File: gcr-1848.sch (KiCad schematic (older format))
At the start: 12 parts, among them U1 LT6010

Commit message: Annotated some components and added a few Greek letters
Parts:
- C1: value 0.1uF -> 0.1μF
- C2, C3: value 33uF -> 33μF
- R3, R4: renamed from R?; value 220M -> 220MΩ
- gave numbers to parts that had none: 2
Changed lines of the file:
@@
 $EndComp
 $Comp
-L US_R R?
+L US_R R4
 U 1 1 5B46BAAD
 P 4350 3825
-F 0 "R?" H 4350 3725 60  0000 C CNN
-F 1 "220M" H 4350 3925 60  0000 C CNN
+F 0 "R4" H 4350 3725 60  0000 C CNN
+F 1 "220MΩ" H 4350 3925 60  0000 C CNN
 F 2 "" H 4350 3925 60  0001 C CNN
 F 3 "" H 4350 3925 60  0001 C CNN
@@
 $EndComp
 $Comp
-L US_R R?
+L US_R R3
 U 1 1 5B46BF5B
 P 4175 3250
-F 0 "R?" H 4175 3150 60  0000 C CNN
-F 1 "220M" H 4175 3350 60  0000 C CNN
+F 0 "R3" H 4175 3150 60  0000 C CNN
+F 1 "220MΩ" H 4175 3350 60  0000 C CNN
 F 2 "" H 4175 3350 60  0001 C CNN
 F 3 "" H 4175 3350 60  0001 C CNN
@@
 P 4575 5125
 F 0 "C1" H 4575 5000 60  0000 C CNN
-F 1 "0.1uF" H 4575 5250 60  0000 C CNN
+F 1 "0.1μF" H 4575 5250 60  0000 C CNN
 F 2 "" H 4575 5250 60  0001 C CNN
 F 3 "" H 4575 5250 60  0001 C CNN
@@
 $EndComp
 $Comp
-L CAPSL C?
+L CAPSL C4
 U 1 1 5B46D889
 P 4100 4350
-F 0 "C?" H 4100 4200 60  0000 C CNN
+F 0 "C4" H 4100 4200 60  0000 C CNN
 F 1 "CPLT" H 4100 4500 60  0000 C CNN
 F 2 "" H 4100 4475 60  0001 C CNN
@@
 $EndComp
 $Comp
-L XLR_MALE J?
+L XLR_MALE J1
 U 1 1 5B46DD1A
 P 4200 6700
-F 0 "J?" H 4200 6925 60  0000 C CNN
+F 0 "J1" H 4200 6925 60  0000 C CNN
 F 1 "XLR_MALE" H 4200 6475 60  0000 C CNN
 F 2 "" H 4200 6700 60  0001 C CNN
@@
 P 4650 6675
 F 0 "C3" H 4650 6550 60  0000 C CNN
-F 1 "33uF" H 4650 6800 60  0000 C CNN
+F 1 "33μF" H 4650 6800 60  0000 C CNN
 F 2 "" H 4650 6800 60  0001 C CNN
 F 3 "" H 4650 6800 60  0001 C CNN
@@
 P 3775 6025
 F 0 "C2" H 3775 5900 60  0000 C CNN
-F 1 "33uF" H 3775 6150 60  0000 C CNN
+F 1 "33μF" H 3775 6150 60  0000 C CNN
 F 2 "" H 3775 6150 60  0001 C CNN
 F 3 "" H 3775 6150 60  0001 C CNN

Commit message: Laid out components on PCB
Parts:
- C1: footprint (none) -> Capacitors_SMD:C_0805
- C2, C3: footprint (none) -> Capacitors_SMD:C_2220
- D1, D2: footprint (none) -> Diodes_SMD:SOD-123
- R1, R2, R3, R4: footprint (none) -> Resistors_SMD:R_0805
- U1: footprint (none) -> Housings_SOIC:SOIC-8_3.9x4.9mm_Pitch1.27mm
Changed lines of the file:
@@
 $EndDescr
 $Comp
-L Earth #PWR?
+L Earth #PWR01
 U 1 1 5B46BA91
 P 4100 4475
-F 0 "#PWR?" H 4100 4225 50  0001 C CNN
+F 0 "#PWR01" H 4100 4225 50  0001 C CNN
 F 1 "Earth" H 4100 4325 50  0001 C CNN
 F 2 "" H 4100 4475 50  0000 C CNN
@@
 F 0 "R4" H 4350 3725 60  0000 C CNN
 F 1 "220MΩ" H 4350 3925 60  0000 C CNN
-F 2 "" H 4350 3925 60  0001 C CNN
+F 2 "Resistors_SMD:R_0805" H 4350 3925 60  0001 C CNN
 F 3 "" H 4350 3925 60  0001 C CNN
 	1    4350 3825
@@
 F 0 "D2" H 4000 3950 60  0000 C CNN
 F 1 "12V" H 4000 3700 60  0000 C CNN
-F 2 "" H 4000 3825 60  0001 C CNN
+F 2 "Diodes_SMD:SOD-123" H 4000 3825 60  0001 C CNN
 F 3 "" H 4000 3825 60  0001 C CNN
 	1    4000 3825
@@
 $EndComp
 $Comp
-L Earth #PWR?
+L Earth #PWR02
 U 1 1 5B46BF2C
 P 4000 4000
-F 0 "#PWR?" H 4000 3750 50  0001 C CNN
+F 0 "#PWR02" H 4000 3750 50  0001 C CNN
 F 1 "Earth" H 4000 3850 50  0001 C CNN
 F 2 "" H 4000 4000 50  0000 C CNN
@@
 F 0 "R3" H 4175 3150 60  0000 C CNN
 F 1 "220MΩ" H 4175 3350 60  0000 C CNN
-F 2 "" H 4175 3350 60  0001 C CNN
+F 2 "Resistors_SMD:R_0805" H 4175 3350 60  0001 C CNN
 F 3 "" H 4175 3350 60  0001 C CNN
 	1    4175 3250
@@
 $EndComp
 $Comp
-L Earth #PWR?
+L Earth #PWR03
 U 1 1 5B46C6B1
 P 3875 4950
-F 0 "#PWR?" H 3875 4700 50  0001 C CNN
+F 0 "#PWR03" H 3875 4700 50  0001 C CNN
 F 1 "Earth" H 3875 4800 50  0001 C CNN
 F 2 "" H 3875 4950 50  0000 C CNN
@@
 F 0 "C1" H 4575 5000 60  0000 C CNN
 F 1 "0.1μF" H 4575 5250 60  0000 C CNN
-F 2 "" H 4575 5250 60  0001 C CNN
+F 2 "Capacitors_SMD:C_0805" H 4575 5250 60  0001 C CNN
 F 3 "" H 4575 5250 60  0001 C CNN
 	1    4575 5125
@@
 $EndComp
 $Comp
-L Earth #PWR?
+L Earth #PWR04
 U 1 1 5B46C778
 P 4650 5400
-F 0 "#PWR?" H 4650 5150 50  0001 C CNN
+F 0 "#PWR04" H 4650 5150 50  0001 C CNN
 F 1 "Earth" H 4650 5250 50  0001 C CNN
 F 2 "" H 4650 5400 50  0000 C CNN
@@
 F 0 "U1" H 4300 4970 50  0000 C CNN
 F 1 "LT6010" H 4225 4825 50  0000 L CNN
-F 2 "" H 4175 5075 50  0000 C CNN
+F 2 "Housings_SOIC:SOIC-8_3.9x4.9mm_Pitch1.27mm" H 4175 5075 50  0001 C CNN
 F 3 "" H 4275 5175 50  0000 C CNN
 	1    4225 4975
@@
 $EndComp
 $Comp
-L +24V #PWR?
+L +24V #PWR05
 U 1 1 5B46CDAE
 P 4575 4800
-F 0 "#PWR?" H 4575 4650 50  0001 C CNN
+F 0 "#PWR05" H 4575 4650 50  0001 C CNN
 F 1 "+24V" H 4575 4940 50  0000 C CNN
 F 2 "" H 4575 4800 50  0000 C CNN
@@
 $EndComp
 $Comp
-L +24V #PWR?
+L +24V #PWR06
 U 1 1 5B46D01F
 P 4175 3000
-F 0 "#PWR?" H 4175 2850 50  0001 C CNN
+F 0 "#PWR06" H 4175 2850 50  0001 C CNN
 F 1 "+24V" H 4175 3140 50  0000 C CNN
 F 2 "" H 4175 3000 50  0000 C CNN
@@
 F 0 "R1" H 4100 5925 60  0000 C CNN
 F 1 "6.8k" H 4100 6125 60  0000 C CNN
-F 2 "" H 4100 6125 60  0001 C CNN
+F 2 "Resistors_SMD:R_0805" H 4100 6125 60  0001 C CNN
 F 3 "" H 4100 6125 60  0001 C CNN
 	1    4100 6025
@@
 F 0 "R2" H 4850 5925 60  0000 C CNN
 F 1 "6.8k" H 4850 6125 60  0000 C CNN
-F 2 "" H 4850 6125 60  0001 C CNN
+F 2 "Resistors_SMD:R_0805" H 4850 6125 60  0001 C CNN
 F 3 "" H 4850 6125 60  0001 C CNN
 	1    4850 6025
@@
 F 0 "D1" H 4475 6150 60  0000 C CNN
 F 1 "24V" H 4475 5900 60  0000 C CNN
-F 2 "" H 4475 6025 60  0001 C CNN
+F 2 "Diodes_SMD:SOD-123" H 4475 6025 60  0001 C CNN
 F 3 "" H 4475 6025 60  0001 C CNN
 	1    4475 6025
@@
 $EndComp
 $Comp
-L Earth #PWR?
+L Earth #PWR07
 U 1 1 5B46F6F9
 P 4475 6200
-F 0 "#PWR?" H 4475 5950 50  0001 C CNN
+F 0 "#PWR07" H 4475 5950 50  0001 C CNN
 F 1 "Earth" H 4475 6050 50  0001 C CNN
 F 2 "" H 4475 6200 50  0000 C CNN
@@
 F 0 "C3" H 4650 6550 60  0000 C CNN
 F 1 "33μF" H 4650 6800 60  0000 C CNN
-F 2 "" H 4650 6800 60  0001 C CNN
+F 2 "Capacitors_SMD:C_2220" H 4650 6800 60  0001 C CNN
 F 3 "" H 4650 6800 60  0001 C CNN
 	1    4650 6675
@@
 F 0 "C2" H 3775 5900 60  0000 C CNN
 F 1 "33μF" H 3775 6150 60  0000 C CNN
-F 2 "" H 3775 6150 60  0001 C CNN
+F 2 "Capacitors_SMD:C_2220" H 3775 6150 60  0001 C CNN
 F 3 "" H 3775 6150 60  0001 C CNN
 	1    3775 6025
@@
 $EndComp
 $Comp
-L Earth #PWR?
+L Earth #PWR08
 U 1 1 5B470768
 P 4325 7150
-F 0 "#PWR?" H 4325 6900 50  0001 C CNN
+F 0 "#PWR08" H 4325 6900 50  0001 C CNN
 F 1 "Earth" H 4325 7000 50  0001 C CNN
 F 2 "" H 4325 7150 50  0000 C CNN
@@
 $EndComp
 $Comp
-L +24V #PWR?
+L +24V #PWR09
 U 1 1 5B46F7CA
 P 4275 5625
-F 0 "#PWR?" H 4275 5475 50  0001 C CNN
+F 0 "#PWR09" H 4275 5475 50  0001 C CNN
 F 1 "+24V" H 4275 5765 50  0000 C CNN
 F 2 "" H 4275 5625 50  0000 C CNN

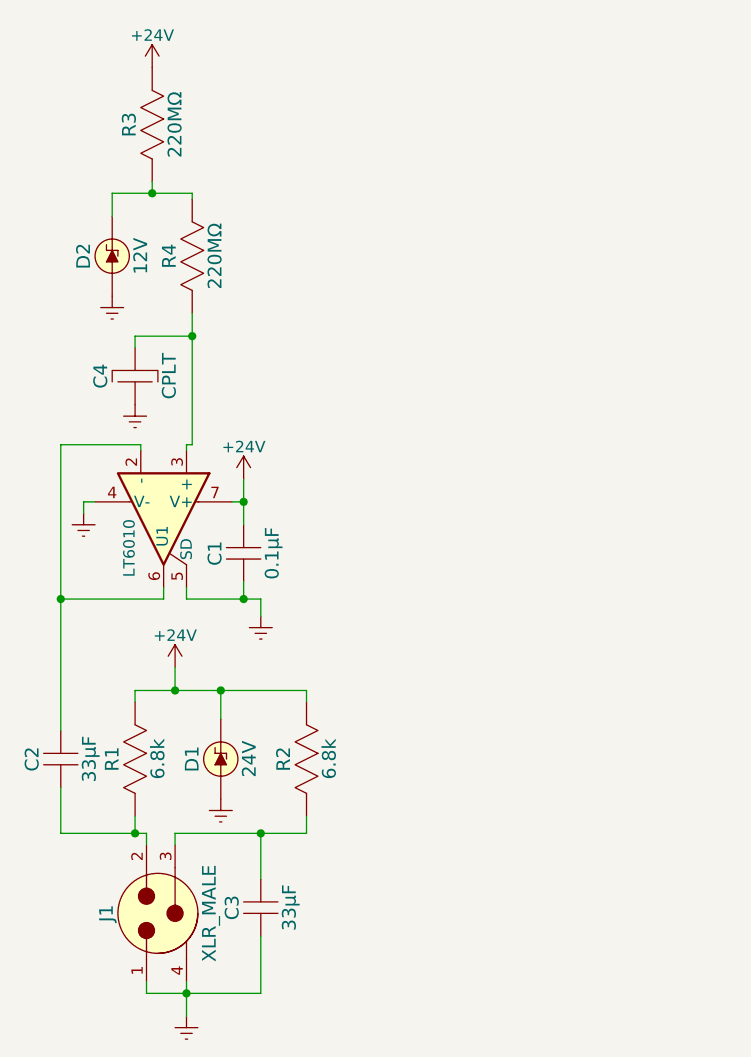
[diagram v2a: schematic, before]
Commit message: Updated PCB and rearranged schematic
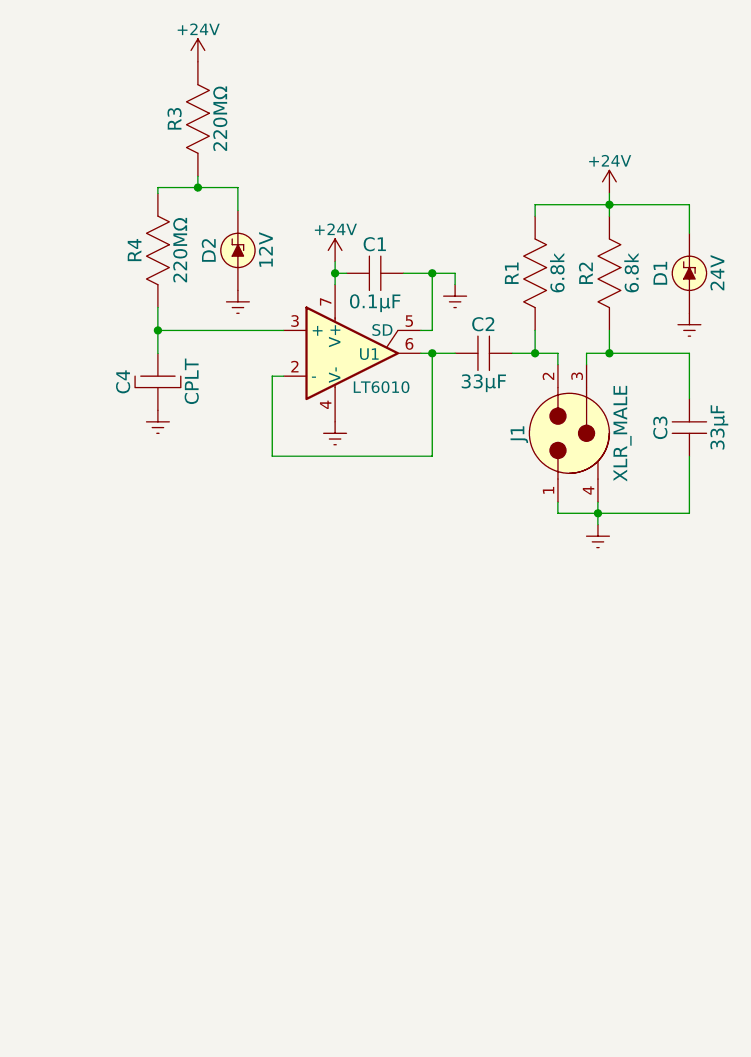
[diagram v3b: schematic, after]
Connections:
- net +24V: now also C1.2; no longer C1.1
- net Earth: now also C1.1, C4.1; no longer C1.2, C4.2
- net at R4.2, U1.3 (+): now also C4.2; no longer C4.1
- net at U1.2 (-), U1.6: now also C2.2; no longer C2.1
- net at J1.2, R1.2: now also C2.1; no longer C2.2
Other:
- moved on the sheet: C1, C2, C3, C4, D1, D2, J1, R1, R2, R3, R4, U1
